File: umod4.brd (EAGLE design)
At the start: 104.9 x 69.8 mm, 101 parts, among them IC1 27C256-FEED-THRU, M1 Generic single-sided NEO-8, M2 RPi Pico W, Q1 DNP/SI2301CDS, Q2 SS8050, U1 RP2040, U2 W25Q128JVSIQ, U3 SY6280AAC, U4 74LVC2G04, U5 74LVC541, U6 74LVC541, U7 74LVC4245, U8 TLV75733P, Y1 12MHz

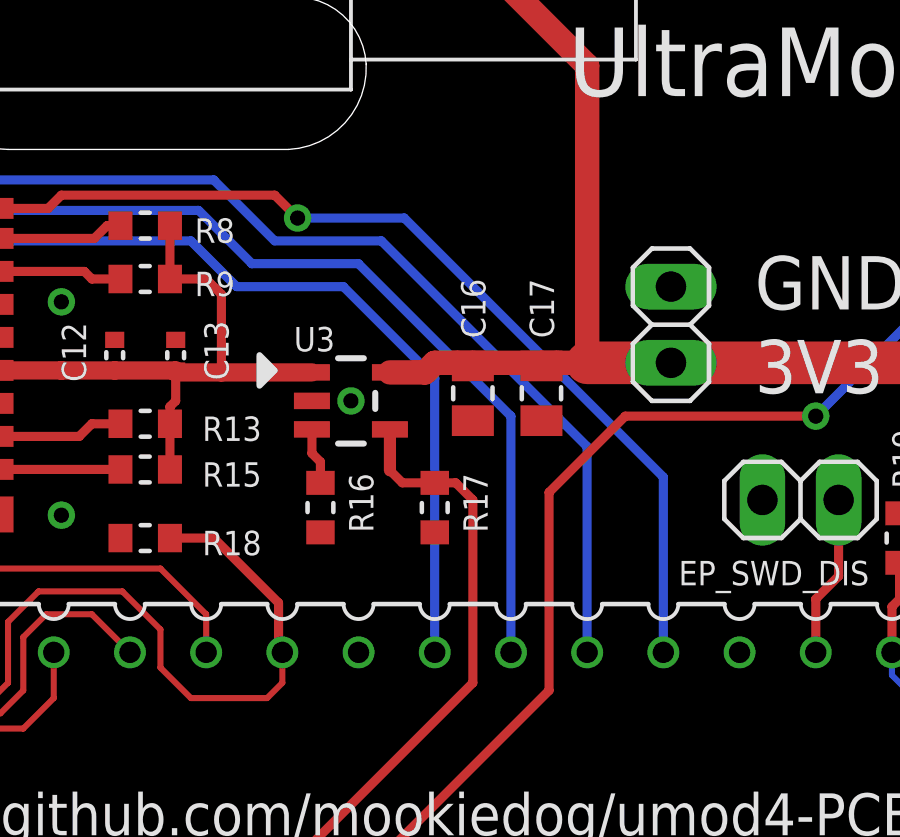
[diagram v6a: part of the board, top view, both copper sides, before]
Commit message: Added test point for VDD_SD
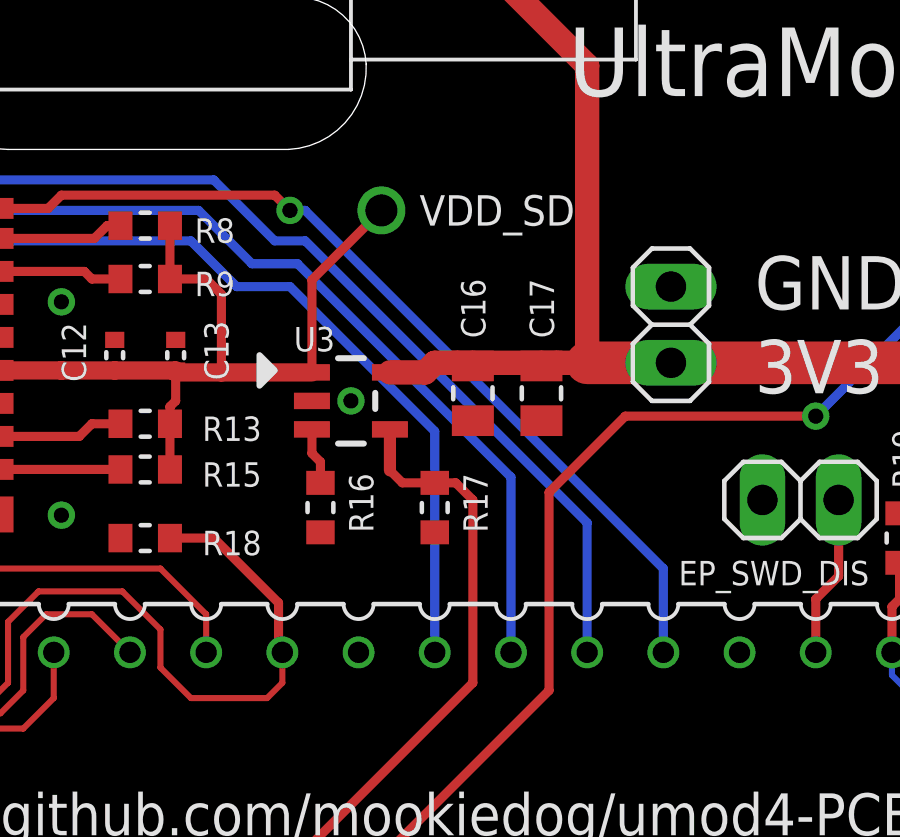
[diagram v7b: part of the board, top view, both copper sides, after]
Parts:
- added TP17: 1035, robins-v7:KEYSTONE-1035
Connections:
- net VDD_SD: now also TP17.P$1
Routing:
- net VDD_SD: track 20.3 -> 26.7 mm
- net !CARD: track 32.2 -> 30.4 mm
- net GPS_PPS: track 52.0 -> 50.5 mm
- net PICOW_U1_TX: track 59.8 -> 58.6 mm
- net PICOW_U1_RX: track 44.8 -> 43.8 mm
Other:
- board text added: "VDD_SD"
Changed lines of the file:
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@@
 <layer number="44" name="Drills" color="7" fill="1" visible="no" active="yes"/>
 <layer number="45" name="Holes" color="7" fill="1" visible="no" active="yes"/>
-<layer number="46" name="Milling" color="3" fill="1" visible="no" active="yes"/>
+<layer number="46" name="Milling" color="3" fill="1" visible="yes" active="yes"/>
 <layer number="47" name="Measures" color="7" fill="1" visible="no" active="yes"/>
 <layer number="48" name="Document" color="7" fill="1" visible="no" active="yes"/>
@@
 <text x="9.906" y="4.318" size="1.27" layer="25" ratio="14">+</text>
 <text x="36.068" y="5.334" size="1.27" layer="25" ratio="14">+</text>
+<text x="33.02" y="40.132" size="1.016" layer="25" font="vector" ratio="14">VDD_SD</text>
 </plain>
 <attributes>
@@
 <attribute name="VALUE" x="1.778" y="55.626" size="0.8128" layer="27" font="vector" ratio="16"/>
 </element>
+<element name="TP17" library="robins-v7" package="KEYSTONE-1035" value="1035" x="31.75" y="40.64" smashed="yes">
+<attribute name="VALUE" x="30.48" y="38.1" size="0.8128" layer="27" font="vector" ratio="16"/>
+</element>
 </elements>
 <signals>
@@
 <wire x1="20.64" y1="40.706" x2="21.082" y2="41.148" width="0.3048" layer="1"/>
 <wire x1="21.082" y1="41.148" x2="28.194" y2="41.148" width="0.3048" layer="1"/>
-<wire x1="28.194" y1="41.148" x2="28.956" y2="40.386" width="0.3048" layer="1"/>
-<via x="28.956" y="40.386" extent="1-16" drill="0.508"/>
-<wire x1="41.148" y1="25.908" x2="41.148" y2="31.75" width="0.3048" layer="16"/>
-<wire x1="41.148" y1="31.75" x2="32.512" y2="40.386" width="0.3048" layer="16"/>
-<wire x1="32.512" y1="40.386" x2="28.956" y2="40.386" width="0.3048" layer="16"/>
+<wire x1="28.194" y1="41.148" x2="28.702" y2="40.64" width="0.3048" layer="1"/>
+<via x="28.702" y="40.64" extent="1-16" drill="0.508"/>
+<wire x1="28.702" y1="40.64" x2="29.21" y2="40.64" width="0.3048" layer="16"/>
+<wire x1="29.21" y1="40.64" x2="41.148" y2="28.702" width="0.3048" layer="16"/>
+<wire x1="41.148" y1="28.702" x2="41.148" y2="25.908" width="0.3048" layer="16"/>
 </signal>
 <signal name="+5_ECU">
@@
 <wire x1="17.018" y1="41.656" x2="26.162" y2="41.656" width="0.3048" layer="16"/>
 <wire x1="26.162" y1="41.656" x2="28.194" y2="39.624" width="0.3048" layer="16"/>
-<wire x1="28.194" y1="39.624" x2="31.75" y2="39.624" width="0.3048" layer="16"/>
-<wire x1="31.75" y1="39.624" x2="38.608" y2="32.766" width="0.3048" layer="16"/>
-<wire x1="38.608" y1="32.766" x2="38.608" y2="25.908" width="0.3048" layer="16"/>
 <wire x1="14.224" y1="55.372" x2="11.303" y2="58.293" width="0.3048" layer="16"/>
 <wire x1="10.414" y1="58.293" x2="11.303" y2="58.293" width="0.3048" layer="16"/>
+<wire x1="28.194" y1="39.624" x2="29.21" y2="39.624" width="0.3048" layer="16"/>
+<wire x1="29.21" y1="39.624" x2="38.608" y2="30.226" width="0.3048" layer="16"/>
+<wire x1="38.608" y1="30.226" x2="38.608" y2="25.908" width="0.3048" layer="16"/>
 </signal>
 <signal name="PICOW_U1_RX">
@@
 <wire x1="16.002" y1="39.624" x2="25.4" y2="39.624" width="0.3048" layer="16"/>
 <wire x1="25.4" y1="39.624" x2="26.924" y2="38.1" width="0.3048" layer="16"/>
-<wire x1="26.924" y1="38.1" x2="30.48" y2="38.1" width="0.3048" layer="16"/>
-<wire x1="30.48" y1="38.1" x2="33.528" y2="35.052" width="0.3048" layer="16"/>
-<wire x1="33.528" y1="35.052" x2="33.528" y2="25.908" width="0.3048" layer="16"/>
 <wire x1="12.192" y1="52.07" x2="11.049" y2="53.213" width="0.3048" layer="16"/>
 <wire x1="10.414" y1="53.213" x2="11.049" y2="53.213" width="0.3048" layer="16"/>
+<wire x1="26.924" y1="38.1" x2="28.702" y2="38.1" width="0.3048" layer="16"/>
+<wire x1="28.702" y1="38.1" x2="33.528" y2="33.274" width="0.3048" layer="16"/>
+<wire x1="33.528" y1="33.274" x2="33.528" y2="25.908" width="0.3048" layer="16"/>
 </signal>
 <signal name="PICOW_U1_TX">
@@
 <wire x1="10.414" y1="55.753" x2="5.969" y2="55.753" width="0.3048" layer="1"/>
 <wire x1="25.654" y1="40.64" x2="27.432" y2="38.862" width="0.3048" layer="16"/>
-<wire x1="27.432" y1="38.862" x2="30.988" y2="38.862" width="0.3048" layer="16"/>
-<wire x1="30.988" y1="38.862" x2="36.068" y2="33.782" width="0.3048" layer="16"/>
-<wire x1="36.068" y1="33.782" x2="36.068" y2="25.908" width="0.3048" layer="16"/>
 <wire x1="13.208" y1="54.102" x2="11.557" y2="55.753" width="0.3048" layer="16"/>
 <wire x1="10.414" y1="55.753" x2="11.557" y2="55.753" width="0.3048" layer="16"/>
+<wire x1="27.432" y1="38.862" x2="28.956" y2="38.862" width="0.3048" layer="16"/>
+<wire x1="28.956" y1="38.862" x2="36.068" y2="31.75" width="0.3048" layer="16"/>
+<wire x1="36.068" y1="31.75" x2="36.068" y2="25.908" width="0.3048" layer="16"/>
 </signal>
 <signal name="SPI1_SCK">
@@
 <wire x1="21.084" y1="35.304" x2="21.082" y2="35.306" width="0.6096" layer="1"/>
 <wire x1="22.86" y1="35.304" x2="24.892" y2="35.304" width="0.6096" layer="1"/>
+<contactref element="TP17" pad="P$1"/>
+<wire x1="29.4339" y1="35.24" x2="29.4339" y2="38.3239" width="0.3048" layer="1"/>
+<wire x1="29.4339" y1="38.3239" x2="31.75" y2="40.64" width="0.3048" layer="1"/>
 </signal>
 <signal name="EP_BOOTSEL">
